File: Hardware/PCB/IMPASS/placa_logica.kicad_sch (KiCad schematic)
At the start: 35 parts, among them J17 PUENTE H_1, J18 PUENTE H_2, J19 SOLENOIDES, J20 SENSORES, J21 PROG, Q67 2N7002, Q68 2N7002, Q69 2N7002, SW1 RESET, SW2 BOOT, U10 LIS3DH, U13 MCP3008, U14 ESP32-S3-WROOM-1, U9 LM75B

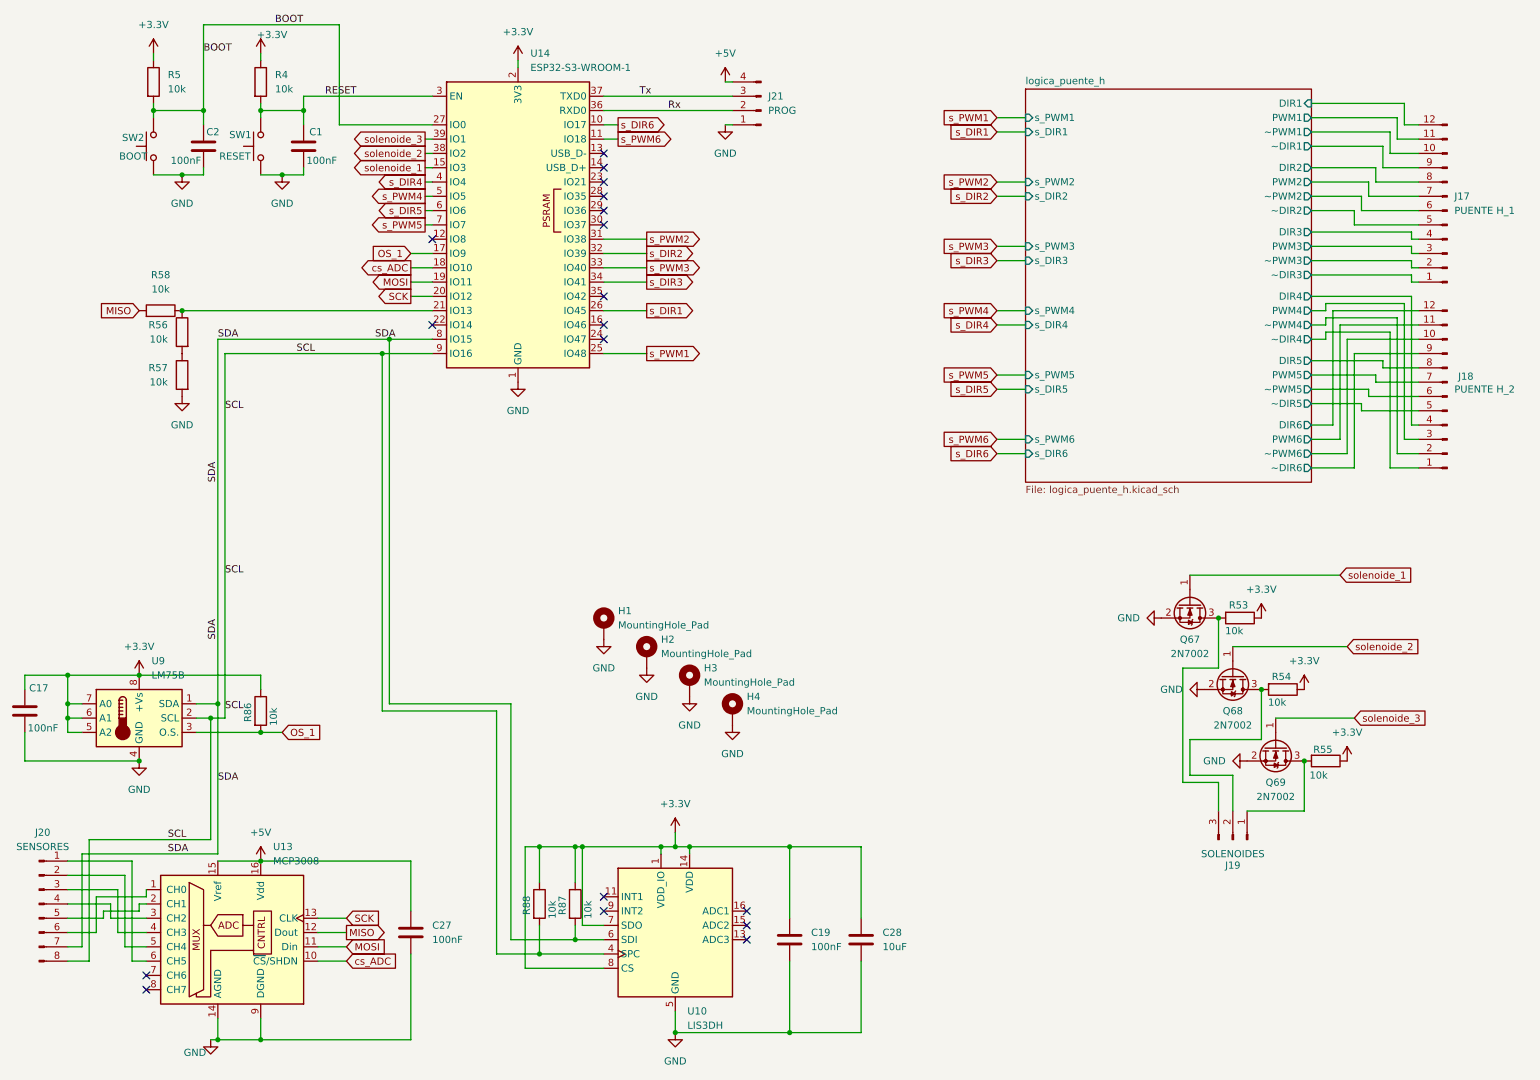
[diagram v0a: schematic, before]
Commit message: Hardware: Update all the logic pcb 	- added ads1015 	- added the logic foe P-MOSFET 	- added I2C connector
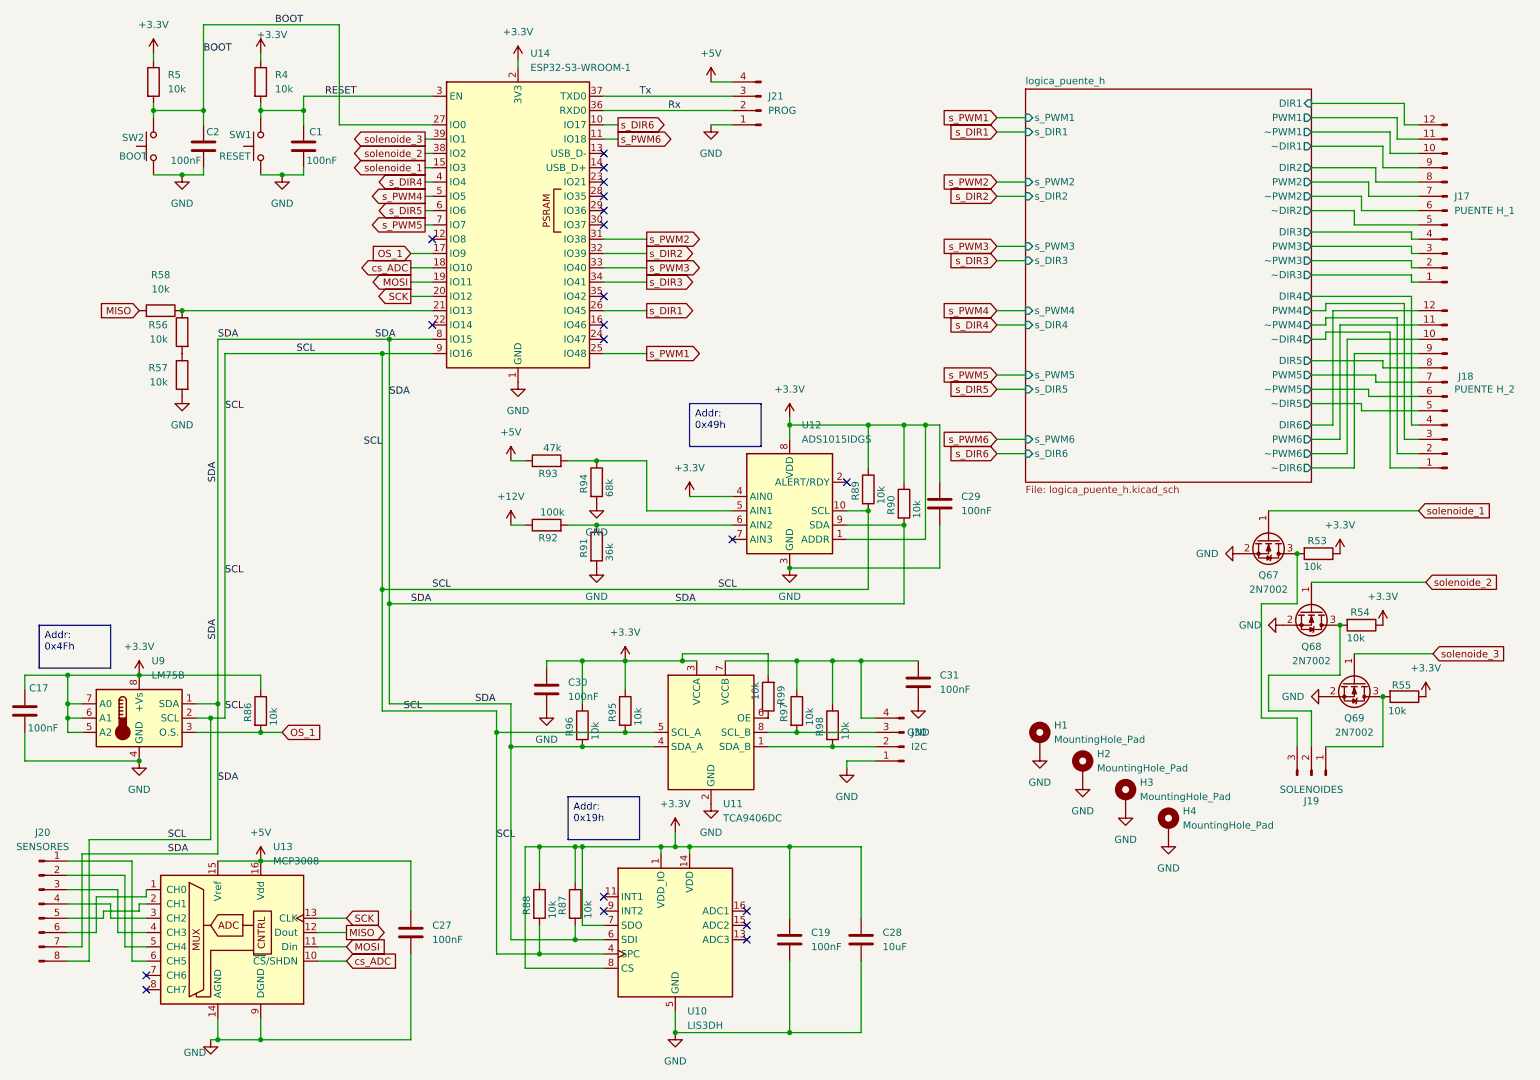
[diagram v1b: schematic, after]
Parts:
- added C29, C30, C31: 100nF, Capacitor_SMD:C_0603_1608Metric, symbol Device:C
- added J30: I2C, Connector_PinHeader_2.54mm:PinHeader_1x04_P2.54mm_Horizontal, symbol Connector:Conn_01x04_Pin
- added R89, R90, R95, R96, R97, R98, R99: 10k, Resistor_SMD:R_0603_1608Metric, symbol Device:R
- added R91: 36k, Resistor_SMD:R_0603_1608Metric, symbol Device:R
- added R92: 100k, Resistor_SMD:R_0603_1608Metric, symbol Device:R
- added R93: 47k, Resistor_SMD:R_0603_1608Metric, symbol Device:R
- added R94: 68k, Resistor_SMD:R_0603_1608Metric, symbol Device:R
- added U11: TCA9406DC, Package_SO:SSOP-8_2.95x2.8mm_P0.65mm, symbol Interface:TCA9406DC
- added U12: ADS1015IDGS, Package_SO:TSSOP-10_3x3mm_P0.5mm, symbol Analog_ADC:ADS1015IDGS
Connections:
- net +3.3V: now also C29.1, C30.1, R89.1, R90.1, R95.1, R96.1, R99.2, U11.3 (VCCA), U12.1 (ADDR), U12.4 (AIN0), U12.8 (VDD)
- net +5V: now also R93.1
- net GND: now also C29.2, C30.2, C31.2, J30.1 (Pin_1), R91.2, R94.2, U11.2 (GND), U12.3 (GND)
- net SCL: now also R89.2, R95.2, U11.5 (SCL_A), U12.10 (SCL)
- net SDA: now also R90.2, R96.2, U11.4 (SDA_A), U12.9 (SDA)
- new net: R93.2, R94.1, U12.5 (AIN1)
- new net: C31.1, J30.4 (Pin_4), R97.1, R98.1, U11.7 (VCCB)
- new net: J30.2 (Pin_2), R98.2, U11.1 (SDA_B)
- new net: J30.3 (Pin_3), R97.2, U11.8 (SCL_B)
- new net: R99.1, U11.6 (OE)
- new net: R91.1, R92.2, U12.6 (AIN2)
- new net +12V: R92.1
- no-connect marks 18 -> 20
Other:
- moved on the sheet: H1, H2, H3, H4, J19, Q67, Q68, Q69, R53, R54, R55

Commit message: Hardware: Update all the power pcb 	- added thr MOSFETs         - added the current sensors         - added the lm75 sensor
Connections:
- net SDA_b: now reaches J30.2 (Pin_2), R98.2, U11.1 (SDA_B)
- net SCL_b: now reaches J30.3 (Pin_3), R97.2, U11.8 (SCL_B)
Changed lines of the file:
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@@
+		)
+	)
+	(label "SCL_b"
+		(at 163.83 139.7 0)
+		(effects
+			(font
+				(size 1.27 1.27)
+			)
+			(justify left bottom)
 		)
 	)
@@
 		(effects
 			(font
+				(size 1.27 1.27)
+			)
+			(justify left bottom)
+		)
+	)
+	(label "SDA_b"
+		(at 153.67 142.24 0)
+		(effects
+			(font
